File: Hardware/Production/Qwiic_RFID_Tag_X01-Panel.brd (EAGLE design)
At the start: 30.5 x 44.5 mm, 48 parts, among them J1 Qwiic, J2 Qwiic, U1 ST25DV64KC

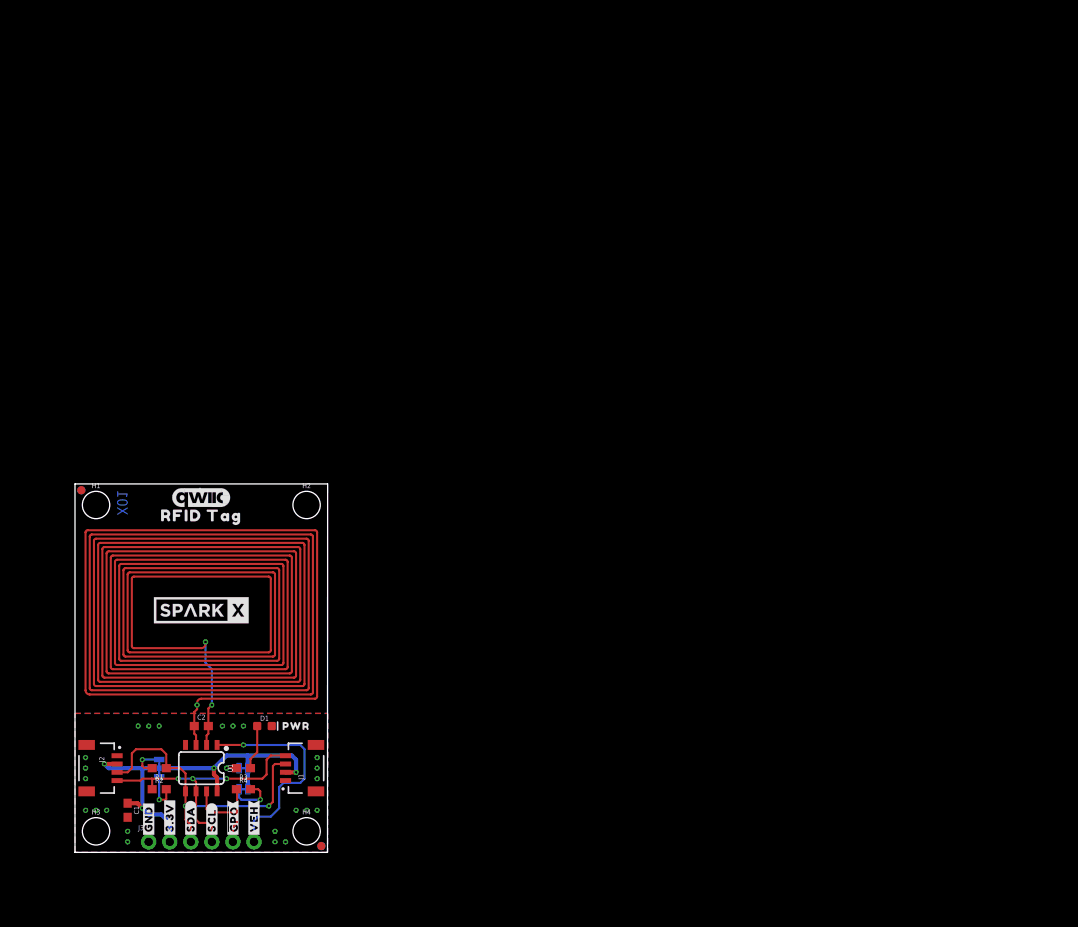
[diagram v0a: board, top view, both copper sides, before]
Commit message: Renamed file to reflect version. Added PCB version to bottom silk.
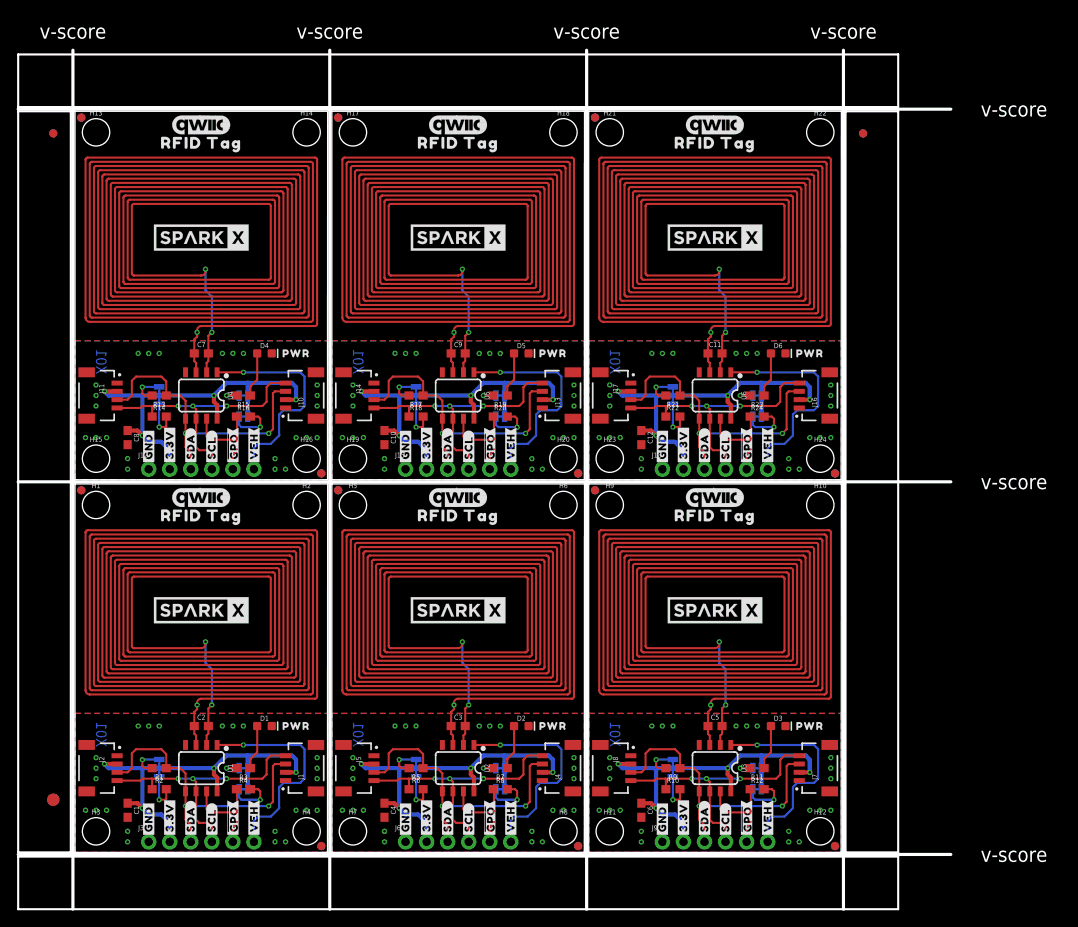
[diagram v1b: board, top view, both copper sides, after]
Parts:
- added C10, C12, C4, C6, C8: 0.1uF, SparkFun-Capacitors:0603
- added C11, C3, C5, C7, C9: 4.7pF, SparkFun-Capacitors:0603
- added D2, D3, D4, D5, D6: RED, SparkFun-LED:LED-0603
- added E$1, E$2, E$3, E$4: (no value), SparkFun-Aesthetics:FIDUCIAL-1X2
- added E$5, E$6: (no value), SparkFun-Retired:FIDUCIAL-1.5X3
- added FD10, FD11, FD12, FD13, FD14, FD15, FD16, FD17, FD18, FD19, FD20, FD21, FD22, FD23, FD24, FD5, FD6, FD7, FD8, FD9: FIDUCIAL1X2, SparkFun-Aesthetics:FIDUCIAL-1X2
- added FRAME2, FRAME3, FRAME4, FRAME5, FRAME6: FRAME-LETTERNO_PACKAGE, SparkFun-Aesthetics:DUMMY
- added H10, H11, H12, H13, H14, H15, H16, H17, H18, H19, H20, H21, H22, H23, H24, H5, H6, H7, H8, H9: STAND-OFF, SparkFun-Hardware:STAND-OFF
- added J10, J11, J13, J14, J16, J17, J4, J5, J7, J8: Qwiic, SparkFun-Connectors:JST04_1MM_RA
- added J12, J15, J18, J6, J9: (no value), SparkFun-Connectors:1X06_NO_SILK
- added JP10, JP13, JP16, JP4, JP7: JUMPER-SMT_3_2-NC_TRACE_SILK, SparkFun-Jumpers:SMT-JUMPER_3_2-NC_TRACE_SILK
- added JP11, JP12, JP14, JP15, JP17, JP18, JP5, JP6, JP8, JP9: JUMPER-SMT_2_NC_TRACE_SILK, SparkFun-Jumpers:SMT-JUMPER_2_NC_TRACE_SILK
- added L2, L3, L4, L5, L6: PCB_4UH_INDUCTOR, SparkFun-Coils:PCB_4UH_INDUCTOR
- added LOGO10, LOGO13, LOGO16, LOGO4, LOGO7: OSHW-LOGOMINI, SparkFun-Aesthetics:OSHW-LOGO-MINI
- added LOGO11, LOGO12, LOGO14, LOGO15, LOGO17, LOGO18, LOGO5, LOGO6, LOGO8, LOGO9: QWIIC_LOGO_7MM, SparkFun-Aesthetics:QWIIC_7MM
- added R10, R13, R14, R17, R18, R21, R22, R5, R6, R9: 2.2k, SparkFun-Resistors:0603
- added R11, R15, R19, R23, R7: 1k, SparkFun-Resistors:0603
- added R12, R16, R20, R24, R8: 10k, SparkFun-Resistors:0603
- added U$10, U$110, U$132, U$44, U$66, U$88: (no value), numbers:PCB#16329163281
- added U$100, U$122, U$34, U$56, U$78: (no value), output:##GPO##9
- added U$101, U$123, U$35, U$57, U$79: (no value), output:#LED#10
- added U$102, U$114, U$124, U$26, U$36, U$48, U$58, U$70, U$80, U$92: (no value), output:#GND#4
- added U$103, U$113, U$125, U$25, U$37, U$47, U$59, U$69, U$81, U$91: (no value), output:#3#3V#0
- added U$104, U$115, U$126, U$27, U$38, U$49, U$60, U$71, U$82, U$93: (no value), output:#SDA#5
- added U$105, U$116, U$127, U$28, U$39, U$50, U$61, U$72, U$83, U$94: (no value), output:#SCL#6
- added U$106, U$117, U$128, U$29, U$40, U$51, U$62, U$73, U$84, U$95: (no value), output:##GPO##8
- added U$107, U$118, U$129, U$30, U$41, U$52, U$63, U$74, U$85, U$96: (no value), output:#VEH#7
- added U$108, U$109, U$130, U$131, U$42, U$43, U$64, U$65, U$86, U$87: (no value), output:RFID_TAG13
- added U$111, U$112, U$13, U$24, U$45, U$46, U$67, U$68, U$89, U$90: SPARKX-LOGO5, SparkX:SPARKX-LARGE
- added U$119, U$31, U$53, U$75, U$97: (no value), output:PWR11
- added U$120, U$32, U$54, U$76, U$98: (no value), output:MADE_IN_THE_USA27
- added U$121, U$33, U$55, U$77, U$99: (no value), output:#I2C#11
- added U2, U3, U4, U5, U6: ST25DV64KC, SparkFun-RF:SO08
- moved LOGO1 27.0 mm to (28.7, 15.2)
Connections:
- new net !GPO!1: J6.5, R8.1, U2.7
- new net !GPO!2: J9.5, R12.1, U3.7
- new net !GPO!3: J12.5, R16.1, U4.7
- new net !GPO!4: J15.5, R20.1, U5.7
- new net !GPO!5: J18.5, R24.1, U6.7
- new net 3.3V1: C4.1, J4.2, J5.2, J6.2, JP4.2, JP5.2, JP6.2, U2.8
- new net 3.3V2: C6.1, J7.2, J8.2, J9.2, JP7.2, JP8.2, JP9.2, U3.8
- new net 3.3V3: C8.1, J10.2, J11.2, J12.2, JP10.2, JP11.2, JP12.2, U4.8
- new net 3.3V4: C10.1, J13.2, J14.2, J15.2, JP13.2, JP14.2, JP15.2, U5.8
- new net 3.3V5: C12.1, J16.2, J17.2, J18.2, JP16.2, JP17.2, JP18.2, U6.8
- new net AC10: C11.2, L6.IN1, U6.2
- new net AC11: C11.1, L6.IN2, U6.3
- new net AC2: C3.2, L2.IN1, U2.2
- new net AC3: C3.1, L2.IN2, U2.3
- new net AC4: C5.2, L3.IN1, U3.2
- new net AC5: C5.1, L3.IN2, U3.3
- new net AC6: C7.2, L4.IN1, U4.2
- new net AC7: C7.1, L4.IN2, U4.3
- new net AC8: C9.2, L5.IN1, U5.2
- new net AC9: C9.1, L5.IN2, U5.3
- new net GND1: C4.2, D2.C, J4.1, J5.1, J6.1, U2.4
- new net GND2: C6.2, D3.C, J7.1, J8.1, J9.1, U3.4
- new net GND3: C8.2, D4.C, J10.1, J11.1, J12.1, U4.4
- new net GND4: C10.2, D5.C, J13.1, J14.1, J15.1, U5.4
- new net GND5: C12.2, D6.C, J16.1, J17.1, J18.1, U6.4
- new net N$10: JP6.1, R8.2
- new net N$11: JP7.3, R9.2
- new net N$12: JP7.1, R10.2
- new net N$13: JP8.1, R11.2
- new net N$14: D3.A, R11.1
- new net N$15: JP9.1, R12.2
- new net N$16: JP10.3, R13.2
- new net N$17: JP10.1, R14.2
- new net N$18: JP11.1, R15.2
- new net N$19: D4.A, R15.1
- new net N$20: JP12.1, R16.2
- new net N$21: JP13.3, R17.2
- new net N$22: JP13.1, R18.2
- new net N$23: JP14.1, R19.2
- new net N$24: D5.A, R19.1
- new net N$25: JP15.1, R20.2
- new net N$26: JP16.3, R21.2
- new net N$27: JP16.1, R22.2
- new net N$28: JP17.1, R23.2
- new net N$29: D6.A, R23.1
- new net N$30: JP18.1, R24.2
- new net N$6: JP4.3, R5.2
- new net N$7: JP4.1, R6.2
- new net N$8: JP5.1, R7.2
- new net N$9: D2.A, R7.1
- new net SCL1: J4.4, J5.4, J6.4, R6.1, U2.6
- new net SCL2: J7.4, J8.4, J9.4, R10.1, U3.6
- new net SCL3: J10.4, J11.4, J12.4, R14.1, U4.6
- new net SCL4: J13.4, J14.4, J15.4, R18.1, U5.6
- new net SCL5: J16.4, J17.4, J18.4, R22.1, U6.6
- new net SDA1: J4.3, J5.3, J6.3, R5.1, U2.5
- new net SDA2: J7.3, J8.3, J9.3, R9.1, U3.5
- new net SDA3: J10.3, J11.3, J12.3, R13.1, U4.5
- new net SDA4: J13.3, J14.3, J15.3, R17.1, U5.5
- new net SDA5: J16.3, J17.3, J18.3, R21.1, U6.5
- new net VEH1: J6.6, U2.1
- new net VEH2: J9.6, U3.1
- new net VEH3: J12.6, U4.1
- new net VEH4: J15.6, U5.1
- new net VEH5: J18.6, U6.1
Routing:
- net 3.3V5: track 0.00 -> 48.7 mm, vias 0 -> 4
- net 3.3V4: track 0.00 -> 48.7 mm, vias 0 -> 4
- net 3.3V3: track 0.00 -> 48.7 mm, vias 0 -> 4
- net 3.3V2: track 0.00 -> 48.7 mm, vias 0 -> 4
- net 3.3V1: track 0.00 -> 48.7 mm, vias 0 -> 4
- net SDA4: track 0.00 -> 37.9 mm, vias 0 -> 2
- net SDA3: track 0.00 -> 37.9 mm, vias 0 -> 2
- net SDA5: track 0.00 -> 37.9 mm, vias 0 -> 2
- net SDA2: track 0.00 -> 37.9 mm, vias 0 -> 2
- net SDA1: track 0.00 -> 37.9 mm, vias 0 -> 2
- net SCL2: track 0.00 -> 33.1 mm, vias 0 -> 3
- net SCL1: track 0.00 -> 33.1 mm, vias 0 -> 3
- net SCL5: track 0.00 -> 33.1 mm, vias 0 -> 3
- net SCL3: track 0.00 -> 33.1 mm, vias 0 -> 3
- net SCL4: track 0.00 -> 33.1 mm, vias 0 -> 3
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- added copper zone on layer 1, net GND1
- added copper zone on layer 16, net GND1
- added copper zone on layer 1, net GND2
- added copper zone on layer 16, net GND2
- added copper zone on layer 1, net GND3
- added copper zone on layer 16, net GND3
- added copper zone on layer 1, net GND4
- added copper zone on layer 16, net GND4
- added copper zone on layer 1, net GND5
- added copper zone on layer 16, net GND5
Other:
- board size 30.5 x 44.5 mm -> 112.5 x 103.6 mm
- board text added: "v-score"
- board text removed: "Dimensions in inches"

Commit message: Added production files; updated BOM.
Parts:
- added U$133: (no value), output:#VEH#7
- added U$134, U$135: (no value), output:RFID_TAG13
- added U$136, U$137: (no value), SER:ST25DV64KC5984
- added U$138: (no value), output:MADE_IN_THE_USA20
- U$10: value (none) -> SPARKX-LOGO5; device numbers:PCB#16329163281 -> SparkX:SPARKX-LARGE
- U$100: device output:##GPO##9 -> output:#VEH#7
- U$101: device output:#LED#10 -> output:PWR11
- U$102: device output:#GND#4 -> output:#I2C#11
- U$103: device output:#3#3V#0 -> output:##GPO##9
- U$104: device output:#SDA#5 -> output:#LED#10
- U$105, U$50: device output:#SCL#6 -> output:#GND#4
- U$106, U$95: device output:##GPO##8 -> output:#3#3V#0
- U$107, U$74: device output:#VEH#7 -> output:#SDA#5
- U$108, U$131: device output:RFID_TAG13 -> output:#SCL#6
- U$109, U$86: device output:RFID_TAG13 -> output:##GPO##8
- U$110: device numbers:PCB#16329163281 -> output:#VEH#7
- U$111, U$112, U$89: value SPARKX-LOGO5 -> (none); device SparkX:SPARKX-LARGE -> output:RFID_TAG13
- U$113, U$91: device output:#3#3V#0 -> SER:ST25DV64KC5984
- U$114: device output:#GND#4 -> SER:ST25DV64KC5984
- U$115: device output:#SDA#5 -> output:MADE_IN_THE_USA20
- U$116, U$94: value (none) -> SPARKX-LOGO5; device output:#SCL#6 -> SparkX:SPARKX-LARGE
- U$117: value (none) -> SPARKX-LOGO5; device output:##GPO##8 -> SparkX:SPARKX-LARGE
- U$118, U$129: device output:#VEH#7 -> output:#3#3V#0
- U$119: device output:PWR11 -> output:#GND#4
- U$120: device output:MADE_IN_THE_USA27 -> output:#SDA#5
- U$121: device output:#I2C#11 -> output:#SCL#6
- U$122: device output:##GPO##9 -> output:##GPO##8
- U$123: device output:#LED#10 -> output:#VEH#7
- U$124: device output:#GND#4 -> output:PWR11
- U$125: device output:#3#3V#0 -> output:#I2C#11
- U$126: device output:#SDA#5 -> output:##GPO##9
- U$127: device output:#SCL#6 -> output:#LED#10
- U$128, U$73: device output:##GPO##8 -> output:#GND#4
- U$13, U$24, U$45, U$67, U$68, U$90: value SPARKX-LOGO5 -> (none); device SparkX:SPARKX-LARGE -> SER:ST25DV64KC5984
- U$130: device output:RFID_TAG13 -> output:#SDA#5
- U$132: device numbers:PCB#16329163281 -> output:##GPO##8
- U$14: value (none) -> SPARKX-LOGO5; device output:MADE_IN_THE_USA27 -> SparkX:SPARKX-LARGE
- U$32: device output:MADE_IN_THE_USA27 -> output:#I2C#11
- U$33: device output:#I2C#11 -> output:##GPO##9
- U$34: device output:##GPO##9 -> output:MADE_IN_THE_USA20
- U$44: device numbers:PCB#16329163281 -> SER:ST25DV64KC5984
- U$46: value SPARKX-LOGO5 -> (none); device SparkX:SPARKX-LARGE -> output:MADE_IN_THE_USA20
- U$47: value (none) -> SPARKX-LOGO5; device output:#3#3V#0 -> SparkX:SPARKX-LARGE
- U$48, U$70: value (none) -> SPARKX-LOGO5; device output:#GND#4 -> SparkX:SPARKX-LARGE
- U$49, U$60: device output:#SDA#5 -> output:#3#3V#0
- U$51, U$84: device output:##GPO##8 -> output:#SDA#5
- U$52, U$85: device output:#VEH#7 -> output:#SCL#6
- U$53: device output:PWR11 -> output:##GPO##8
- U$54: device output:MADE_IN_THE_USA27 -> output:#VEH#7
- U$55: device output:#I2C#11 -> output:PWR11
- U$56: device output:##GPO##9 -> output:#I2C#11
- U$57: device output:#LED#10 -> output:##GPO##9
- U$58: device output:#GND#4 -> output:#LED#10
- U$59: device output:#3#3V#0 -> output:#GND#4
- U$61: device output:#SCL#6 -> output:#SDA#5
- U$62: device output:##GPO##8 -> output:#SCL#6
- U$63: device output:#VEH#7 -> output:##GPO##8
- U$64, U$87: device output:RFID_TAG13 -> output:#VEH#7
- U$66, U$88: device numbers:PCB#16329163281 -> output:RFID_TAG13
- U$69: device output:#3#3V#0 -> output:MADE_IN_THE_USA20
- U$71, U$93: value (none) -> SPARKX-LOGO5; device output:#SDA#5 -> SparkX:SPARKX-LARGE
- U$72, U$83: device output:#SCL#6 -> output:#3#3V#0
- U$75: device output:PWR11 -> output:#SCL#6
- U$76: device output:MADE_IN_THE_USA27 -> output:##GPO##8
- U$77: device output:#I2C#11 -> output:#VEH#7
- U$78: device output:##GPO##9 -> output:PWR11
- U$79: device output:#LED#10 -> output:#I2C#11
- U$80: device output:#GND#4 -> output:##GPO##9
- U$81: device output:#3#3V#0 -> output:#LED#10
- U$82: device output:#SDA#5 -> output:#GND#4
- U$92: device output:#GND#4 -> output:MADE_IN_THE_USA20
- U$96: device output:#VEH#7 -> output:#GND#4
- U$97: device output:PWR11 -> output:#SDA#5
- U$98: device output:MADE_IN_THE_USA27 -> output:#SCL#6
- U$99: device output:#I2C#11 -> output:##GPO##8
- moved U$68 76.1 mm to (77.2, 42.7)
- moved U$67 69.5 mm to (77.2, 42.7)
- moved U$69 62.1 mm to (62.7, 11.7), flipped to the bottom
- moved U$46 54.6 mm to (31.8, 11.7), turned to 90 degrees
- moved U$34 51.7 mm to (0.76, 11.7), turned to 90 degrees
- moved U$113 49.1 mm to (46.2, 87.6), turned to 0 degrees
- moved U$91 49.1 mm to (15.2, 87.6), flipped to the bottom, turned to 0 degrees
- moved U$10 47.9 mm to (46.2, 28.2), flipped to the top, turned to 0 degrees
- moved U$114 47.7 mm to (46.2, 87.6), flipped to the bottom, turned to 0 degrees
- moved U$115 45.3 mm to (31.8, 56.6), flipped to the bottom
- moved U$92 40.4 mm to (0.76, 56.6), flipped to the bottom
- moved U$64 39.4 mm to (83.6, 1.78), flipped to the bottom, turned to 90 degrees
- moved U$86 39.0 mm to (19.1, 46.7), flipped to the bottom, turned to 90 degrees
- moved U$108 38.9 mm to (47.5, 46.7), flipped to the bottom, turned to 90 degrees
- moved U$130 38.9 mm to (75.9, 46.7), flipped to the bottom, turned to 90 degrees
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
